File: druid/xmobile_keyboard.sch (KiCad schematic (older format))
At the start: 12 parts, among them SW10 SW_PUSH, SW2 SW_PUSH, SW3 SW_PUSH, SW4 SW_PUSH, SW5 SW_PUSH, SW6 SW_PUSH, SW7 SW_PUSH, SW8 SW_PUSH, SW9 SW_PUSH

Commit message: - Переделана клавиатура - установлены все корпуса микросхем
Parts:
- removed SW10, SW2, SW3, SW4, SW5, SW6, SW7, SW8, SW9: SW_PUSH, symbol SW_PUSH
- added R24, R25: 10kOmh, Resistors_SMD:R_0603_HandSoldering, symbol R-RESCUE-xmobile
- added R26: 10kOmh, Resistors_SMD:R_0603, symbol R-RESCUE-xmobile
- added U10, U11, U12, U13, U14, U6, U7, U8, U9: switch1, switch1:switch_6x9, symbol switch1
- R21: value 1MOmh -> 10KOmh; footprint (none) -> Resistors_SMD:R_0603_HandSoldering; symbol R -> R-RESCUE-xmobile
- R22, R23: value 1MOmh -> 10kOmh; footprint (none) -> Resistors_SMD:R_0603_HandSoldering; symbol R -> R-RESCUE-xmobile
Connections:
- wire segments 15 -> 27
- no-connect marks 0 -> 9

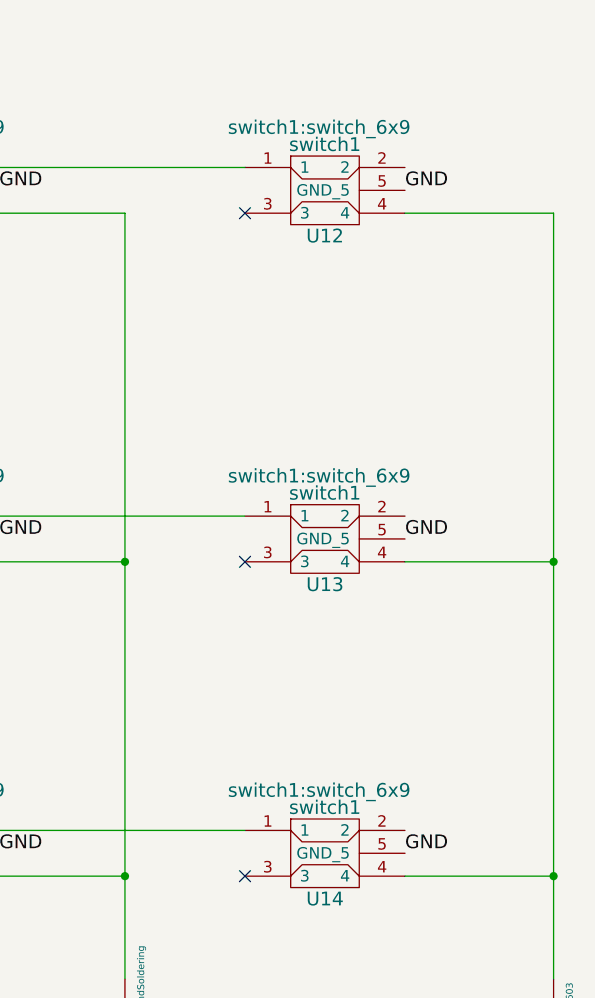
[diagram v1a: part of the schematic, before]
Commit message: Исправлины все ошибки и предупреждения в электрической схеме
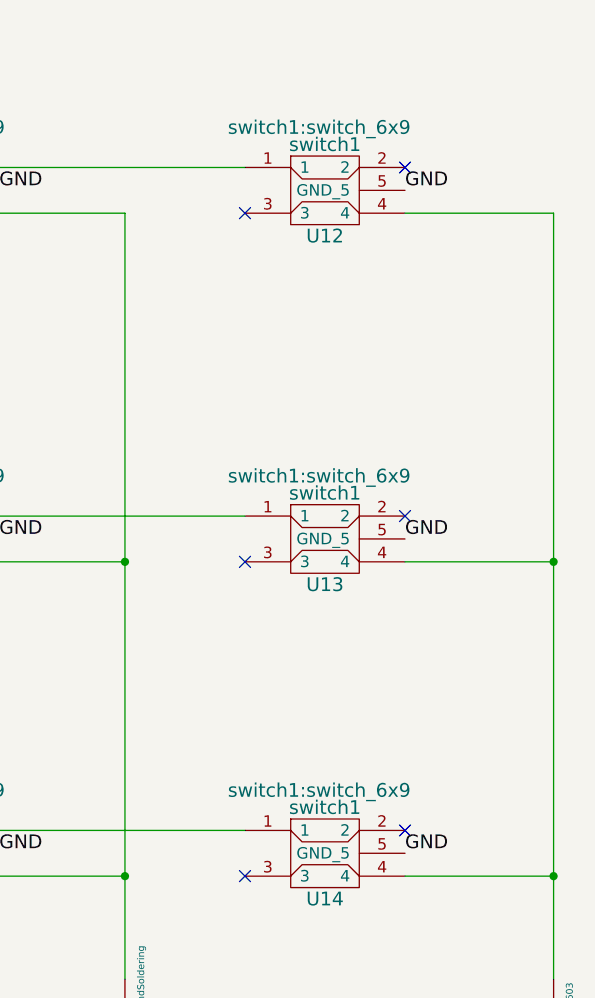
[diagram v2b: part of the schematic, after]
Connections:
- no-connect marks 9 -> 12
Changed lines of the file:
@@
 NoConn ~ 5150 3475
 NoConn ~ 3450 3475
+NoConn ~ 7625 1750
+NoConn ~ 7625 3275
+NoConn ~ 7625 4650
 $EndSCHEMATC

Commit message: Переместил посадочные места по кучкам
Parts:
- R26: footprint Resistors_SMD:R_0603 -> Resistors_SMD:R_0603_HandSoldering
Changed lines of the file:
@@
 F 0 "R26" V 8355 5550 40  0000 C CNN
 F 1 "10kOmh" V 8282 5551 40  0000 C CNN
-F 2 "Resistors_SMD:R_0603" V 8205 5550 30  0000 C CNN
+F 2 "Resistors_SMD:R_0603_HandSoldering" V 8205 5550 30  0000 C CNN
 F 3 "" H 8275 5550 30  0000 C CNN
 	1    8275 5550

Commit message: Всё разведено кроме земель. Площидки надо проверять.
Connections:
- net in1: now also R26.1; no longer R24.1
- net in3: now also R24.1; no longer R26.1
- net out1: now also R23.2; no longer R21.2
- net out3: now also R21.2; no longer R23.2
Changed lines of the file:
@@
 	0    1    1    0
 $EndComp
-Text HLabel 4700 6050 3    60   Input ~ 0
+Text HLabel 8275 6050 3    60   Input ~ 0
 in1
 Text HLabel 6400 6050 3    60   Input ~ 0
 in2
-Text HLabel 8275 6050 3    60   Input ~ 0
+Text HLabel 4700 6050 3    60   Input ~ 0
 in3
-Text HLabel 1800 1750 0    60   Output ~ 0
+Text HLabel 1800 4650 0    60   Output ~ 0
 out1
 Text HLabel 1800 3275 0    60   Output ~ 0
 out2
-Text HLabel 1800 4650 0    60   Output ~ 0
+Text HLabel 1800 1750 0    60   Output ~ 0
 out3
 $Comp

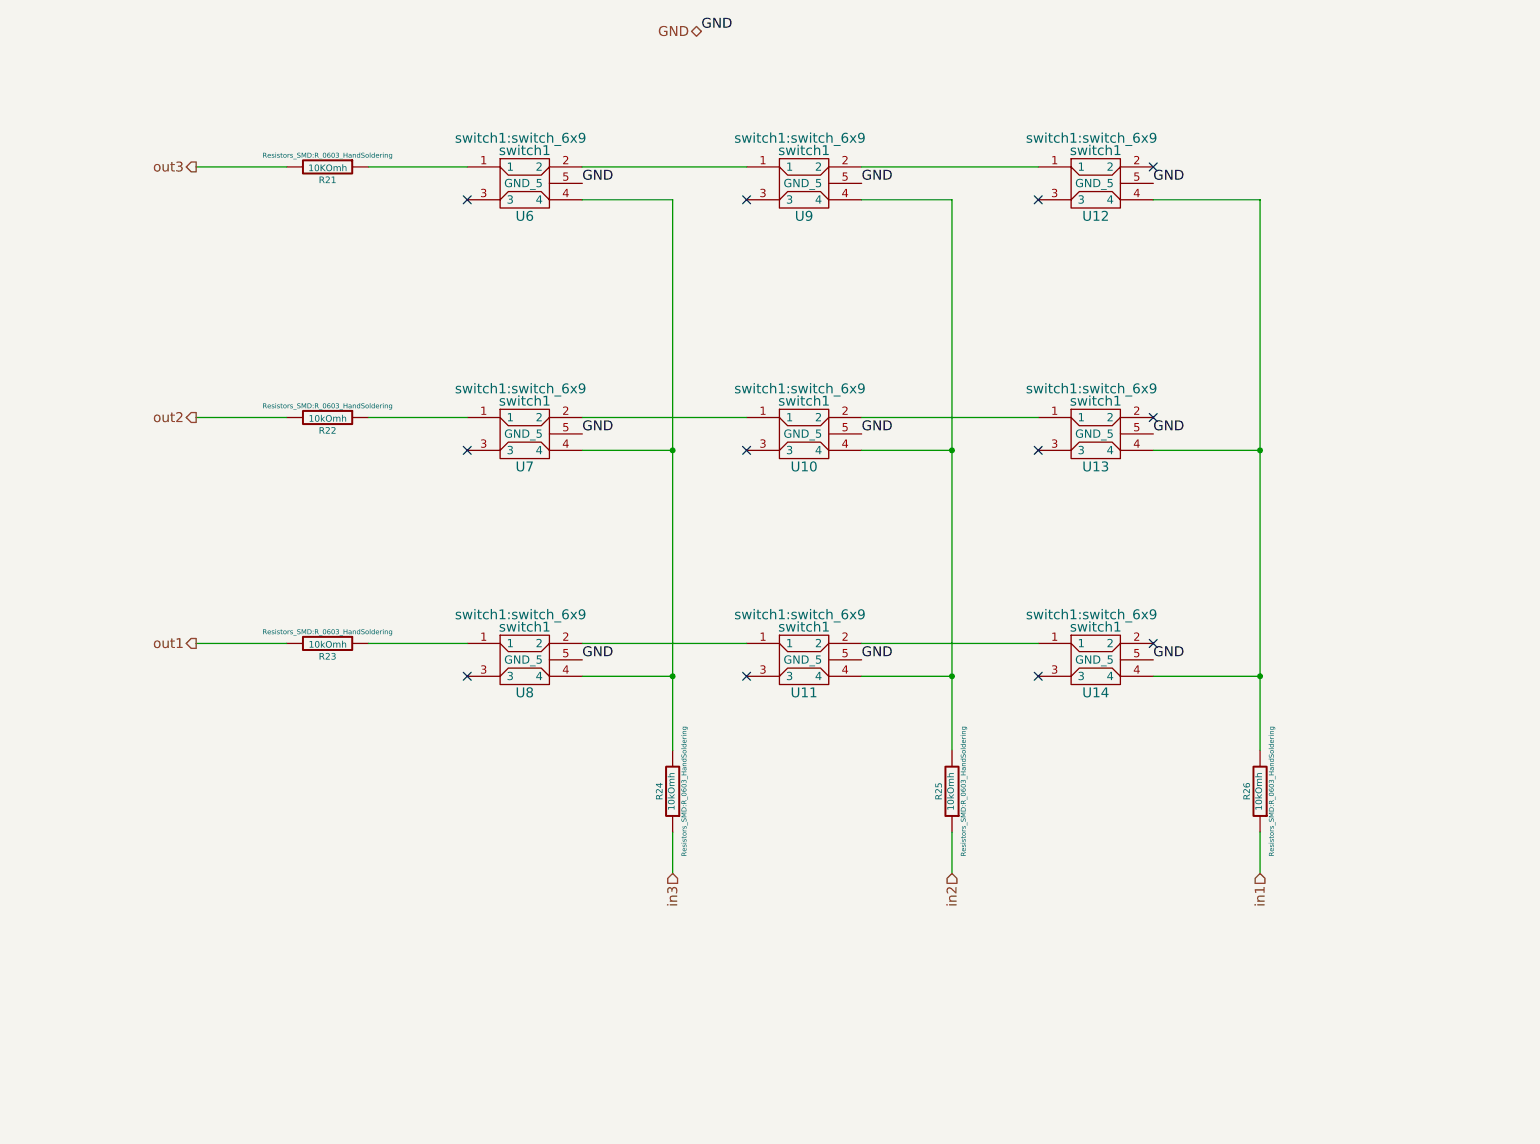
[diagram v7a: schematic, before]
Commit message: + new kbd, but not completed + SRAM lines(labels) replaced by bus
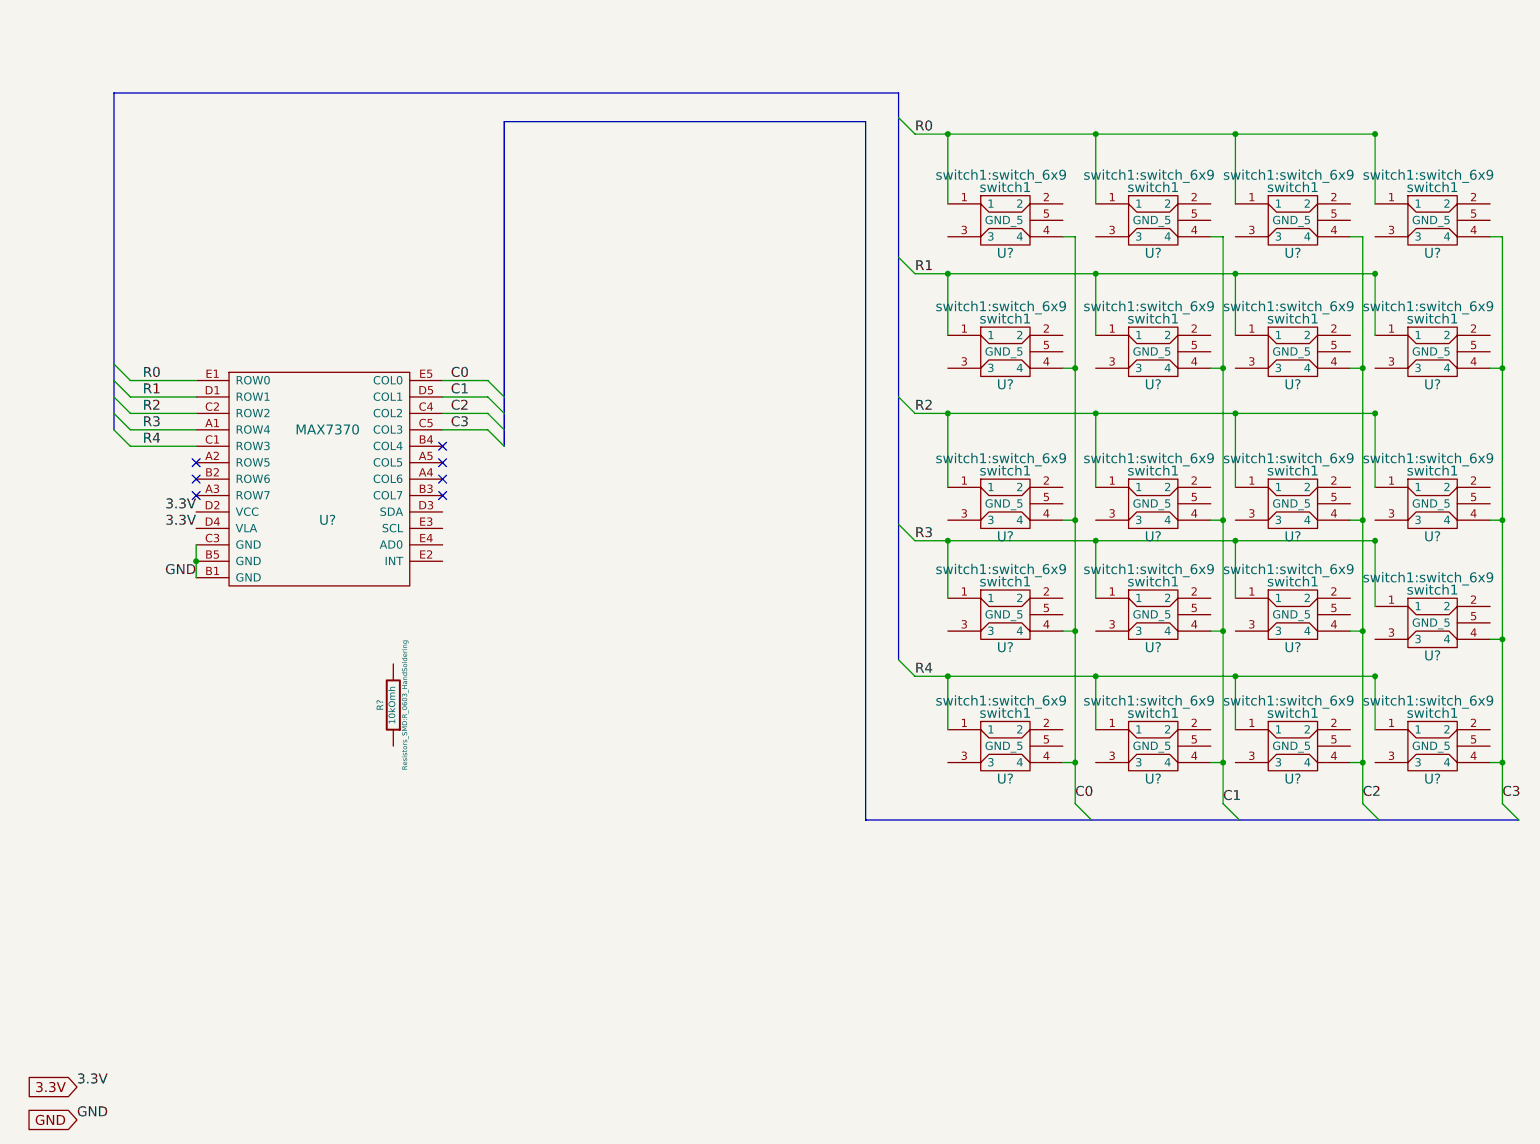
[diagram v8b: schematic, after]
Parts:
- removed R21: 10KOmh, Resistors_SMD:R_0603_HandSoldering, symbol R-RESCUE-xmobile
- removed R22, R23, R24, R25, R26: 10kOmh, Resistors_SMD:R_0603_HandSoldering, symbol R-RESCUE-xmobile
- removed U10, U11, U12, U13, U14, U6, U7, U8, U9: switch1, switch1:switch_6x9, symbol switch1
- added R?: 10kOmh, Resistors_SMD:R_0603_HandSoldering, symbol R-RESCUE-xmobile
- added U?: MAX7370, symbol MAX7370
- added U? (x20): switch1, switch1:switch_6x9, symbol switch1
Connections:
- net GND: now also U?.B1 (GND), U?.B5 (GND), U?.C3 (GND)
- new net 3.3V: U?.D2 (VCC), U?.D4 (VLA)
- new net C0: U?.4, U?.4, U?.4, U?.4, U?.4, U?.E5 (COL0)
- new net C1: U?.4, U?.4, U?.4, U?.4, U?.4, U?.D5 (COL1)
- new net C2: U?.4, U?.4, U?.4, U?.4, U?.4, U?.C4 (COL2)
- new net C3: U?.4, U?.4, U?.4, U?.4, U?.4, U?.C5 (COL3)
- new net R0: U?.1, U?.1, U?.1, U?.1, U?.E1 (ROW0)
- new net R1: U?.1, U?.1, U?.1, U?.1, U?.D1 (ROW1)
- new net R2: U?.1, U?.1, U?.1, U?.1, U?.C2 (ROW2)
- new net R3: U?.1, U?.1, U?.1, U?.1, U?.A1 (ROW4)
- new net R4: U?.1, U?.1, U?.1, U?.1, U?.C1 (ROW3)
- no-connect marks 12 -> 7
